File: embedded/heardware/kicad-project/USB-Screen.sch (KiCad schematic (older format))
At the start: 22 parts, among them J1 USB_B_Micro, J2 Conn_01x04, Q1 NPN, U1 ZJY154T-PG04, U2 CH551, U3 SC662

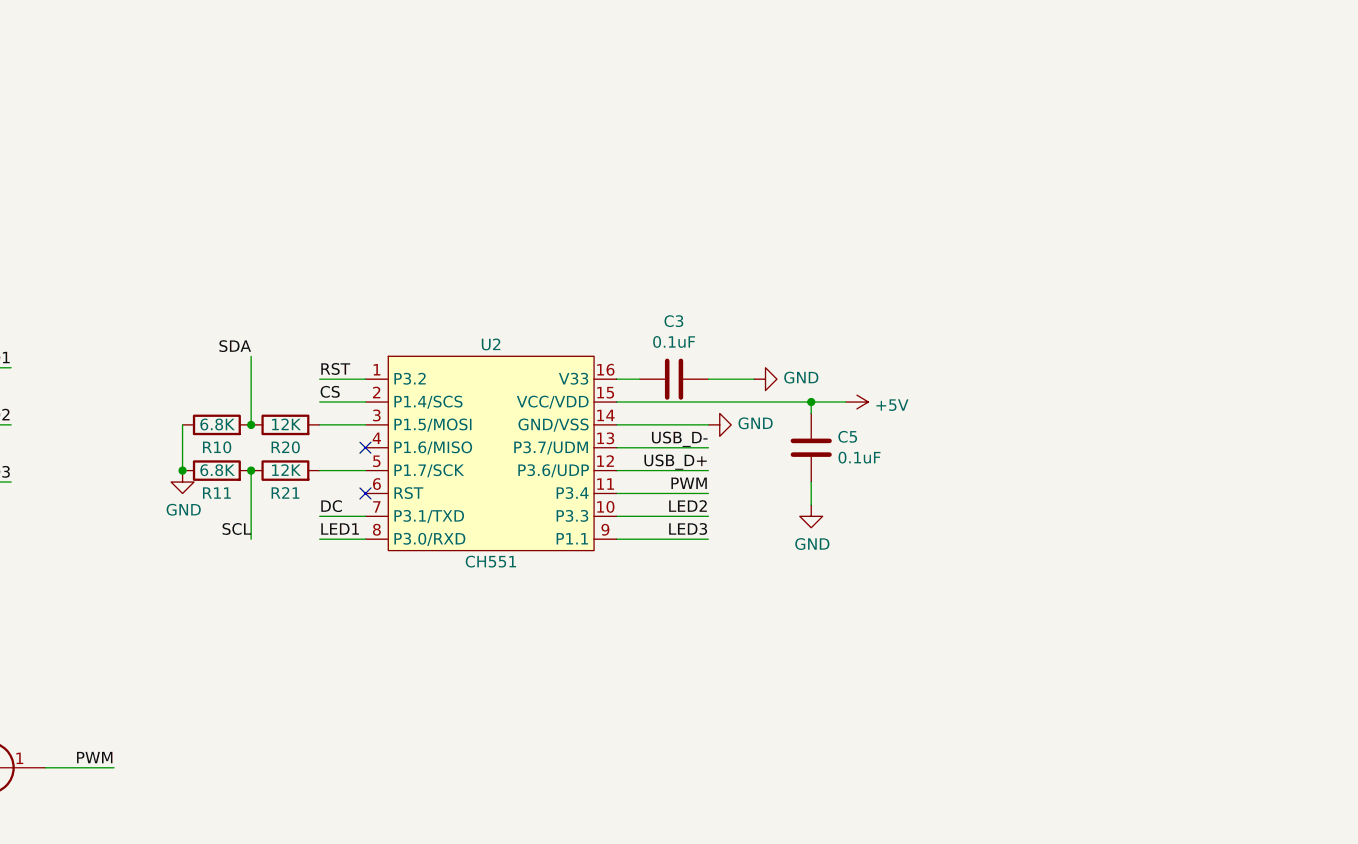
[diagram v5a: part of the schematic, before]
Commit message: 给电路图添加多种备用调试方案
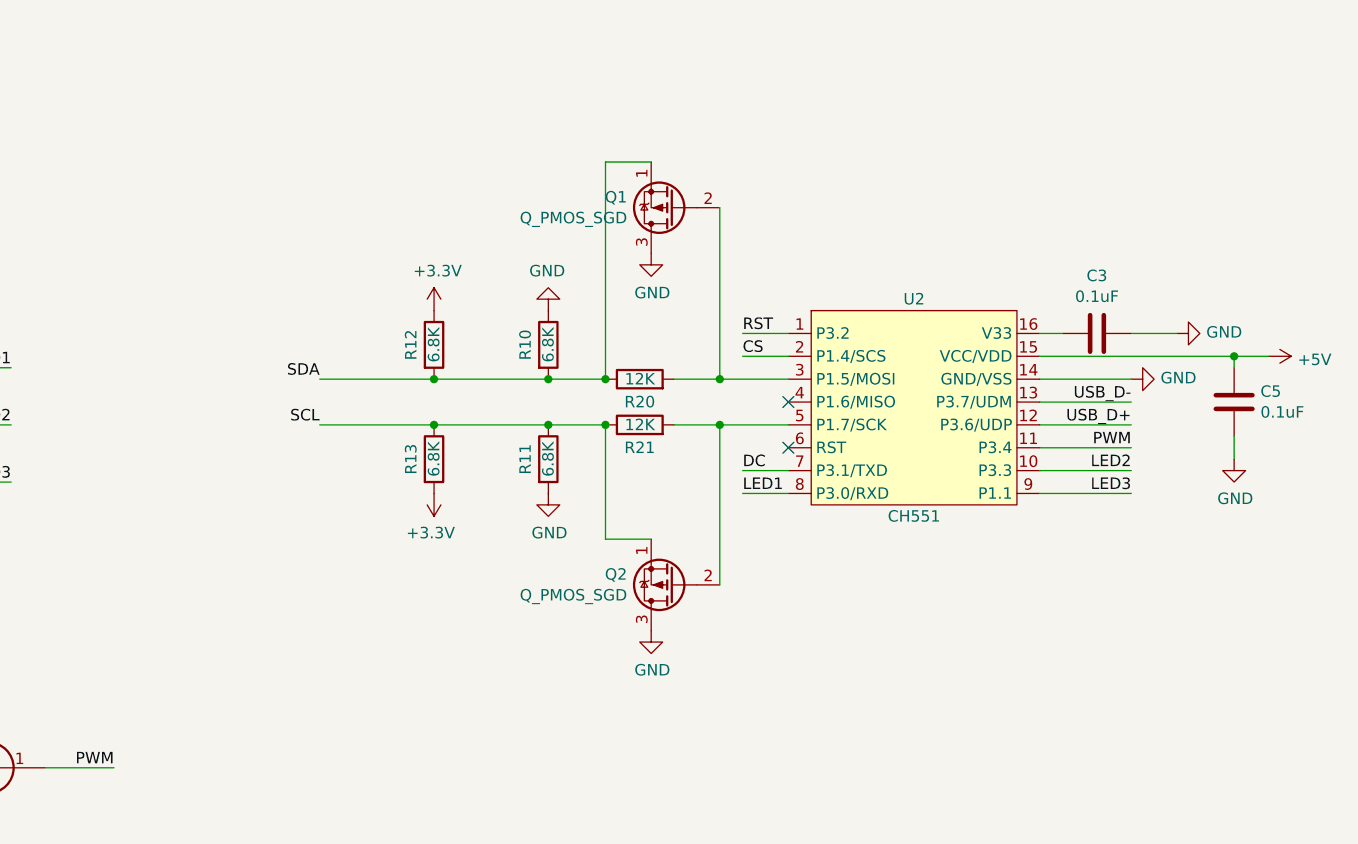
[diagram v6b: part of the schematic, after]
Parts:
- added Q1, Q2: Q_PMOS_SGD, symbol Device:Q_PMOS_SGD
- added R12, R13: 6.8K, Resistor_SMD:R_0402_1005Metric, symbol Device:R
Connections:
- net +3V3: now also R12.1, R13.2
- net GND: now also R11.2, Q1.3 (D), Q2.3 (D); no longer R11.1
- net SCL: now also R11.1, Q2.1 (S), R13.1; no longer R11.2
- net SDA: now also Q1.1 (S), R12.2
- net at R20.2, U2.3 (P1.5/MOSI): now also Q1.2 (G)
- net at R21.2, U2.5 (P1.7/SCK): now also Q2.2 (G)
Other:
- moved on the sheet: C3, C5, R10, R11, R20, R21, U2

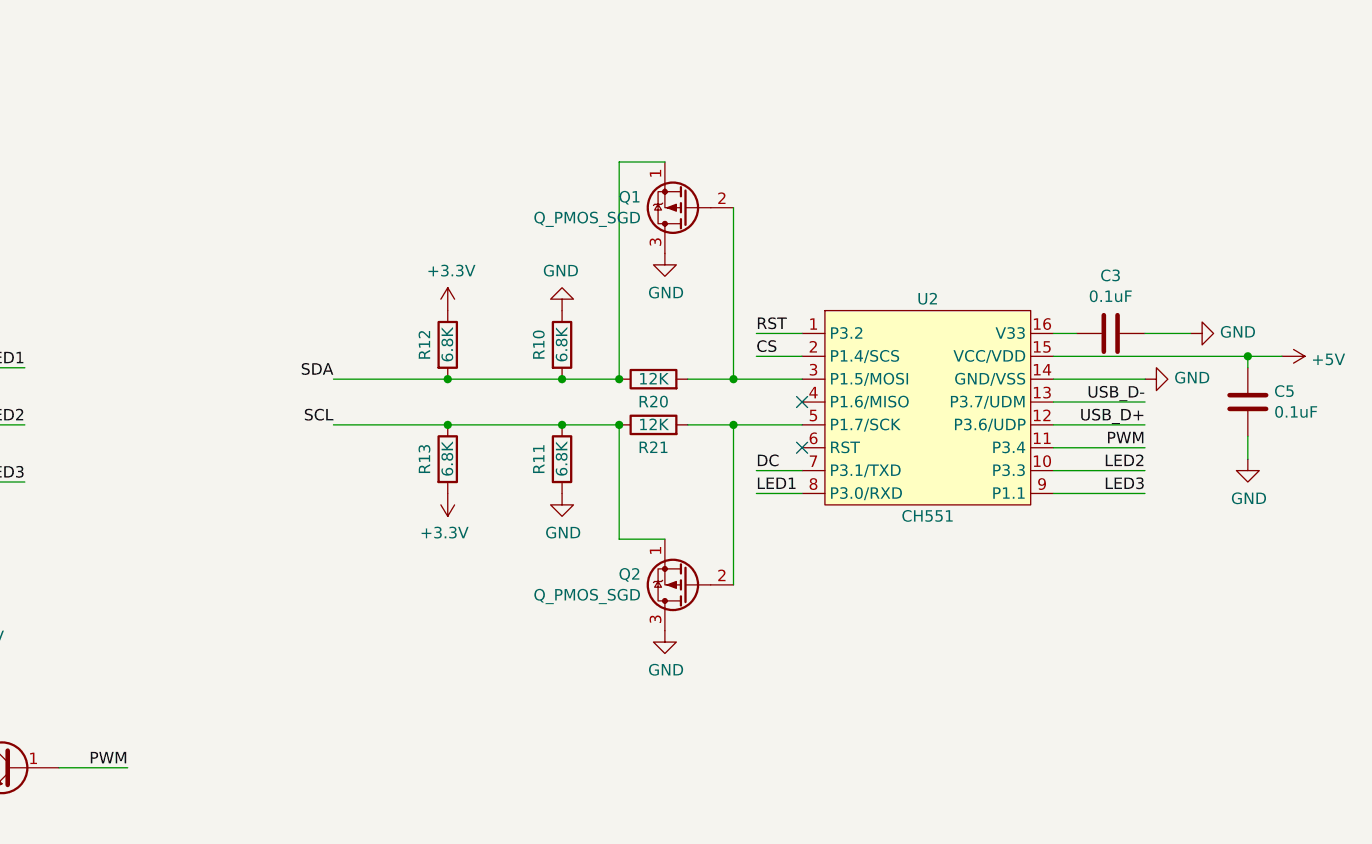
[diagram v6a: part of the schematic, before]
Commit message: 用二极管实现电平转换
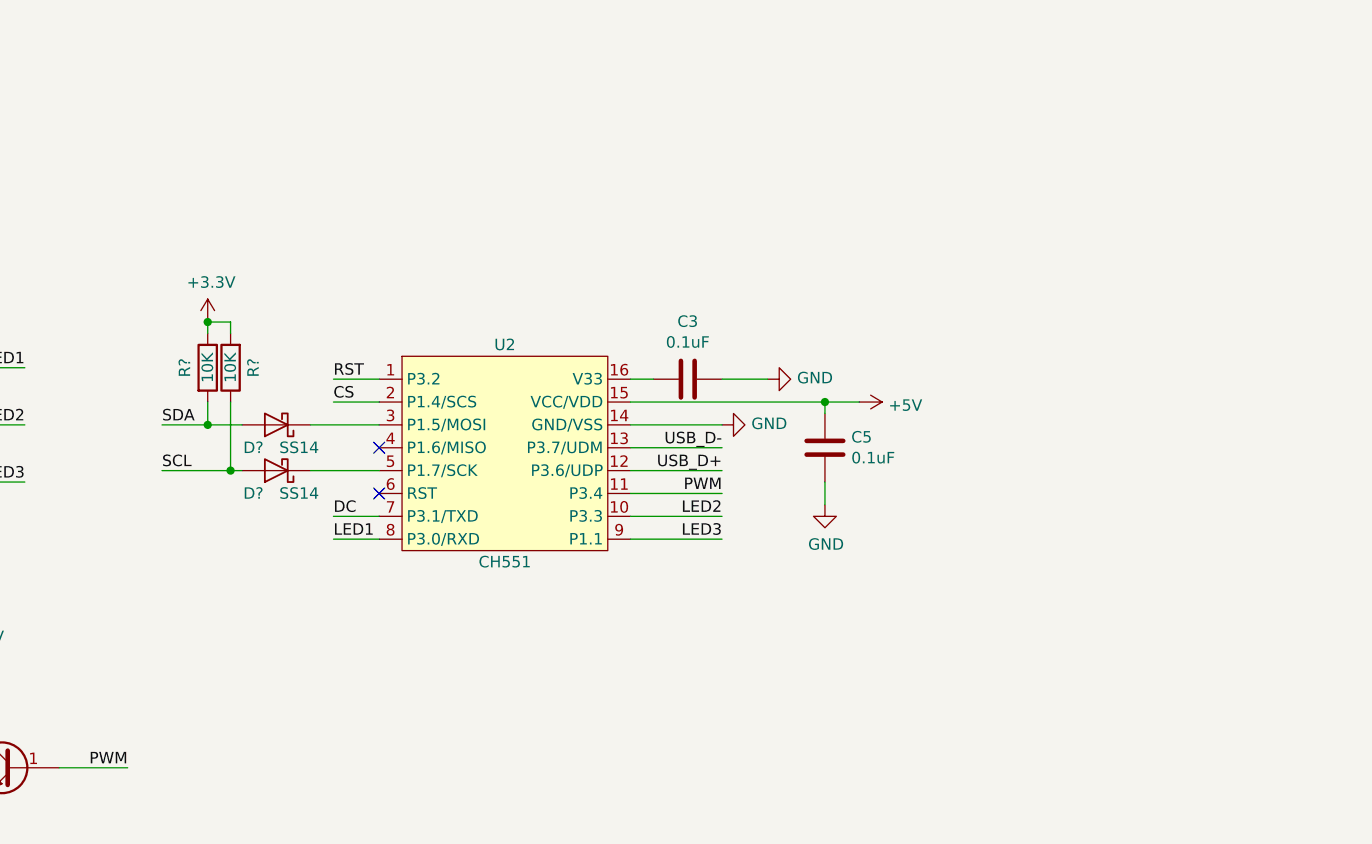
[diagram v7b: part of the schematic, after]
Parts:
- removed Q1, Q2: Q_PMOS_SGD, symbol Device:Q_PMOS_SGD
- removed R10, R11, R12, R13: 6.8K, Resistor_SMD:R_0402_1005Metric, symbol Device:R
- removed R20, R21: 12K, Resistor_SMD:R_0402_1005Metric, symbol Device:R
- added D? (x2): SS14, symbol Device:D_Schottky
- added R? (x2): 10K, Resistor_SMD:R_0402_1005Metric, symbol Device:R
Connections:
- net +3V3: now also R?.1, R?.2
- net SCL: now also D?.2 (A), R?.1
- net SDA: now also D?.2 (A), R?.2
- net at U2.3 (P1.5/MOSI): now also D?.1 (K)
- net at U2.5 (P1.7/SCK): now also D?.1 (K)
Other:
- moved on the sheet: C3, C5, U2

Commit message: 重新布线
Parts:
- D4, D5: renamed from D?; footprint (none) -> Diode_SMD:D_SMA
- gave numbers to parts that had none: 2
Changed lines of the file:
@@
 	4750 5150 5000 5150
 $Comp
-L Device:D_Schottky D?
+L Device:D_Schottky D5
 U 1 1 5F848FB6
 P 6250 3500
-F 0 "D?" H 6350 3600 50  0000 C CNN
+F 0 "D5" H 6350 3600 50  0000 C CNN
 F 1 "SS14" H 6150 3600 50  0000 C CNN
-F 2 "" H 6250 3500 50  0001 C CNN
+F 2 "Diode_SMD:D_SMA" H 6250 3500 50  0001 C CNN
 F 3 "~" H 6250 3500 50  0001 C CNN
 	1    6250 3500
@@
 $EndComp
 $Comp
-L Device:D_Schottky D?
+L Device:D_Schottky D4
 U 1 1 5F84B388
 P 6250 3300
-F 0 "D?" H 6350 3400 50  0000 C CNN
+F 0 "D4" H 6350 3400 50  0000 C CNN
 F 1 "SS14" H 6150 3400 50  0000 C CNN
-F 2 "" H 6250 3300 50  0001 C CNN
+F 2 "Diode_SMD:D_SMA" H 6250 3300 50  0001 C CNN
 F 3 "~" H 6250 3300 50  0001 C CNN
 	1    6250 3300
@@
 SDA
 $Comp
-L Device:R R?
+L Device:R R2
 U 1 1 5F860967
 P 6050 3050
-F 0 "R?" V 5950 3050 50  0000 C CNN
+F 0 "R2" V 5950 3050 50  0000 C CNN
 F 1 "10K" V 6050 3050 50  0000 C CNN
 F 2 "Resistor_SMD:R_0402_1005Metric" V 5980 3050 50  0001 C CNN
@@
 $EndComp
 $Comp
-L Device:R R?
+L Device:R R1
 U 1 1 5F8654DD
 P 5950 3050
-F 0 "R?" V 5850 3050 50  0000 C CNN
+F 0 "R1" V 5850 3050 50  0000 C CNN
 F 1 "10K" V 5950 3050 50  0000 C CNN
 F 2 "Resistor_SMD:R_0402_1005Metric" V 5880 3050 50  0001 C CNN
@@
 	6050 3500 6100 3500
 $Comp
-L power:+3.3V #PWR?
+L power:+3.3V #PWR08
 U 1 1 5F873B8C
 P 5950 2850
-F 0 "#PWR?" H 5950 2700 50  0001 C CNN
+F 0 "#PWR08" H 5950 2700 50  0001 C CNN
 F 1 "+3.3V" H 5965 3023 50  0000 C CNN
 F 2 "" H 5950 2850 50  0001 C CNN
